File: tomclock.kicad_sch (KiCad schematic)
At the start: 5 parts, among them J4 Conn_02x10_Odd_Even, U4 74HCT245

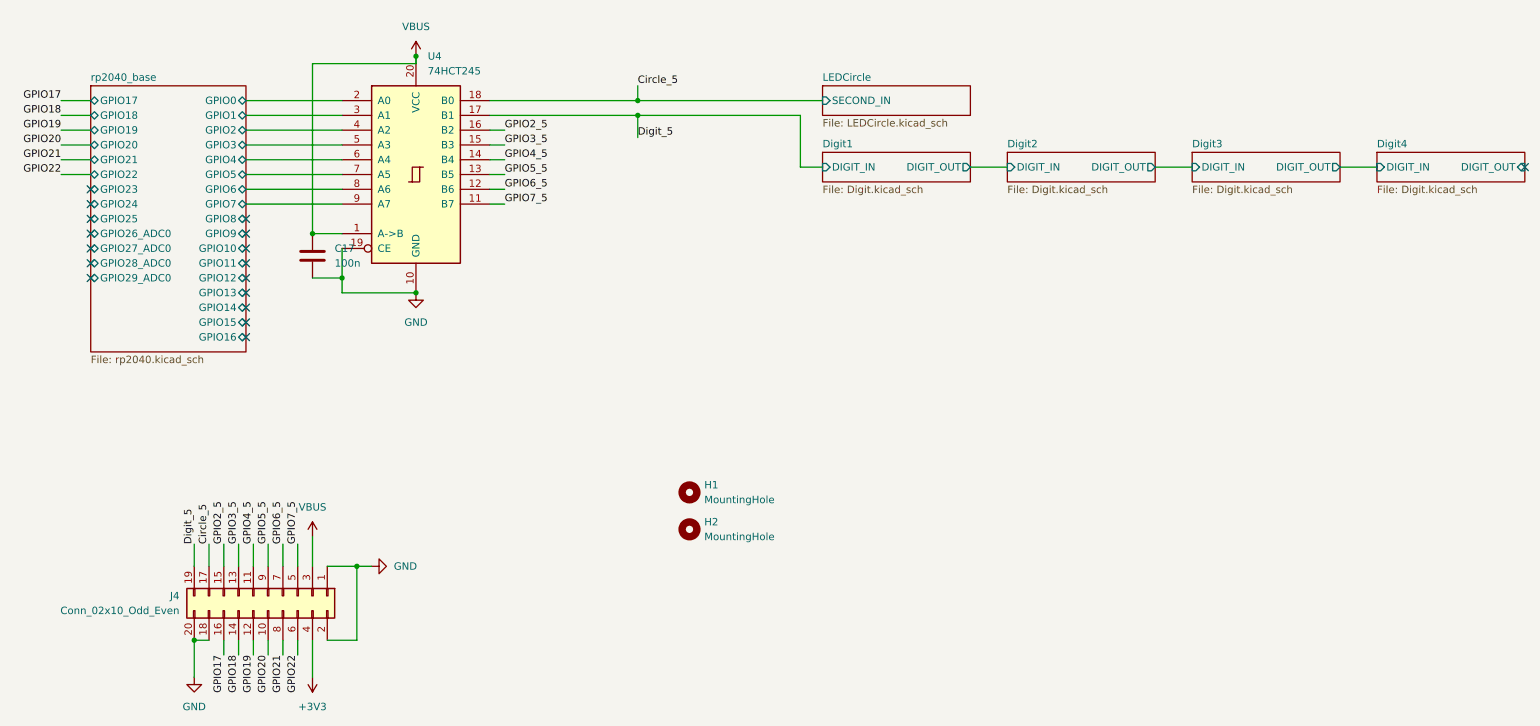
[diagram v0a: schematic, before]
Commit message: Schematic: Update symbols, add esd protection, add I2C header
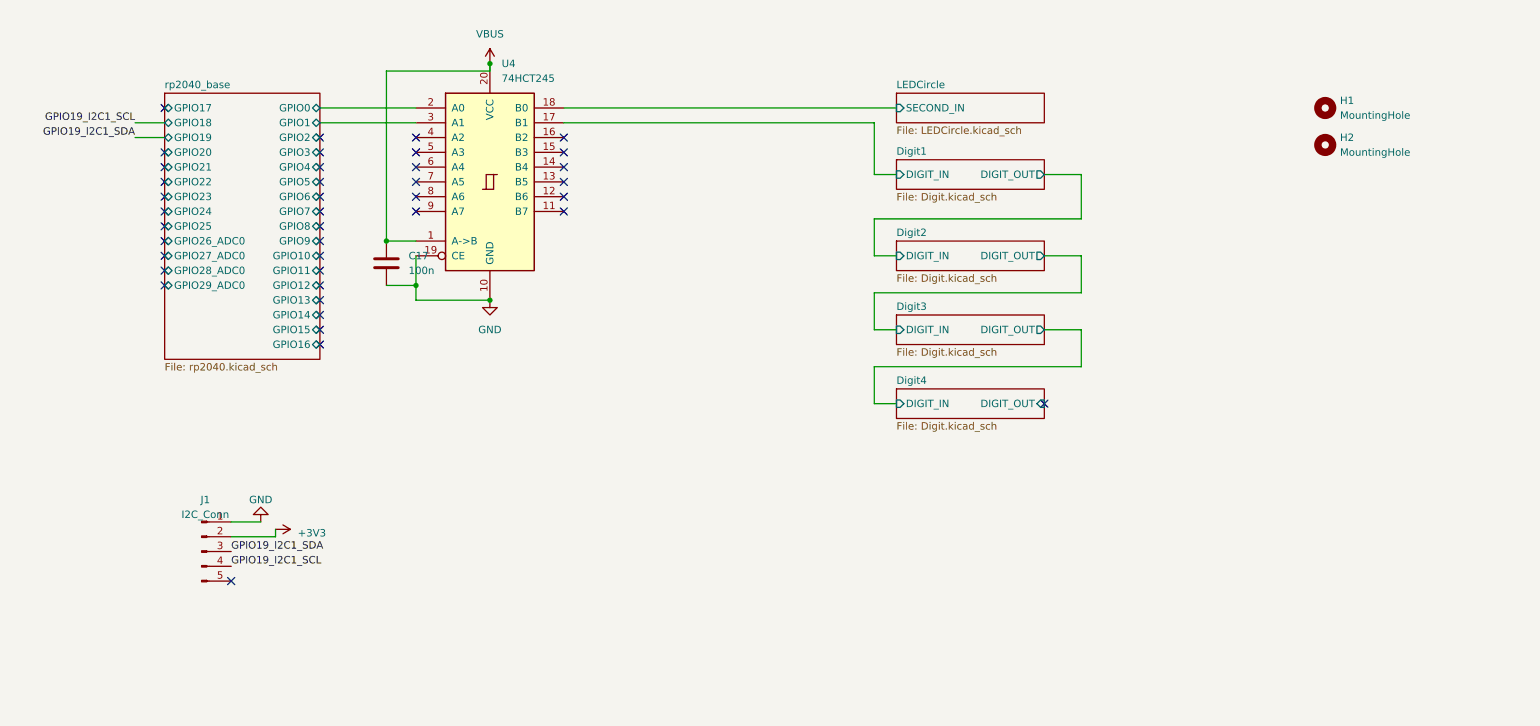
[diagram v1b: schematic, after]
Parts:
- removed J4: Conn_02x10_Odd_Even, Connector_IDC:IDC-Header_2x10_P2.54mm_Vertical, symbol Connector_Generic:Conn_02x10_Odd_Even
- added J1: I2C_Conn, symbol Connector:Conn_01x05_Pin
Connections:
- net +3V3: now also J1.2 (Pin_2)
- net GND: now also J1.1 (Pin_1)
- net rp2040_base/GPIO2: no longer U4.4 (A2)
- net rp2040_base/GPIO3: no longer U4.5 (A3)
- net rp2040_base/GPIO4: no longer U4.6 (A4)
- net rp2040_base/GPIO5: no longer U4.7 (A5)
- net rp2040_base/GPIO6: no longer U4.8 (A6)
- net rp2040_base/GPIO7: no longer U4.9 (A7)
- net Circle_5 renamed LEDCircle/SECOND_IN
- net Digit_5 renamed Digit1/DIGIT_IN
- net GPIO2_5: no longer names the net of U4.16 (B2)
- net GPIO3_5: no longer names the net of U4.15 (B3)
- net GPIO4_5: no longer names the net of U4.14 (B4)
- net GPIO5_5: no longer names the net of U4.13 (B5)
- net GPIO6_5: no longer names the net of U4.12 (B6)
- net GPIO7_5: no longer names the net of U4.11 (B7)
- new net GPIO19_I2C1_SCL: J1.4 (Pin_4)
- new net GPIO19_I2C1_SDA: J1.3 (Pin_3)
- no-connect marks 17 -> 40
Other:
- moved on the sheet: C17, H1, H2, U4

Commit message: PCB: Updated new components, removed old paths
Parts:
- J1: footprint (none) -> Connector_PinHeader_2.54mm:PinHeader_1x05_P2.54mm_Vertical
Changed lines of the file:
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@@
       (effects (font (size 1.27 1.27)))
     )
-    (property "Footprint" "" (at 49.53 106.68 0)
+    (property "Footprint" "Connector_PinHeader_2.54mm:PinHeader_1x05_P2.54mm_Vertical" (at 49.53 106.68 0)
       (effects (font (size 1.27 1.27)) hide)
     )

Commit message: JLC: Fixup for JLC Production
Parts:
- U4: footprint Package_SO:SOIC-20W_7.5x12.8mm_P1.27mm -> esd:SOIC-20_L13.3-W5.5-P1.27-LS7.8-BL; symbol 74xx:74HC245 -> easyeda2kicad:SN74HCT245NSR; JLC Part (none) -> Extended Part; LCSC C5979 -> C133641; LCSC Part (none) -> C133641; Manufacturer (none) -> TI(德州仪器)
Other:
- moved on the sheet: C17

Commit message: Bump kicad version
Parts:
- U4: footprint esd:SOIC-20_L13.3-W5.5-P1.27-LS7.8-BL -> Package_SO:SOIC-20W_7.5x12.8mm_P1.27mm
